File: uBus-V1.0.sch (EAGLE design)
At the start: 13 parts, among them U1 FTS31XS-U, U3 MIC5219 3.3V

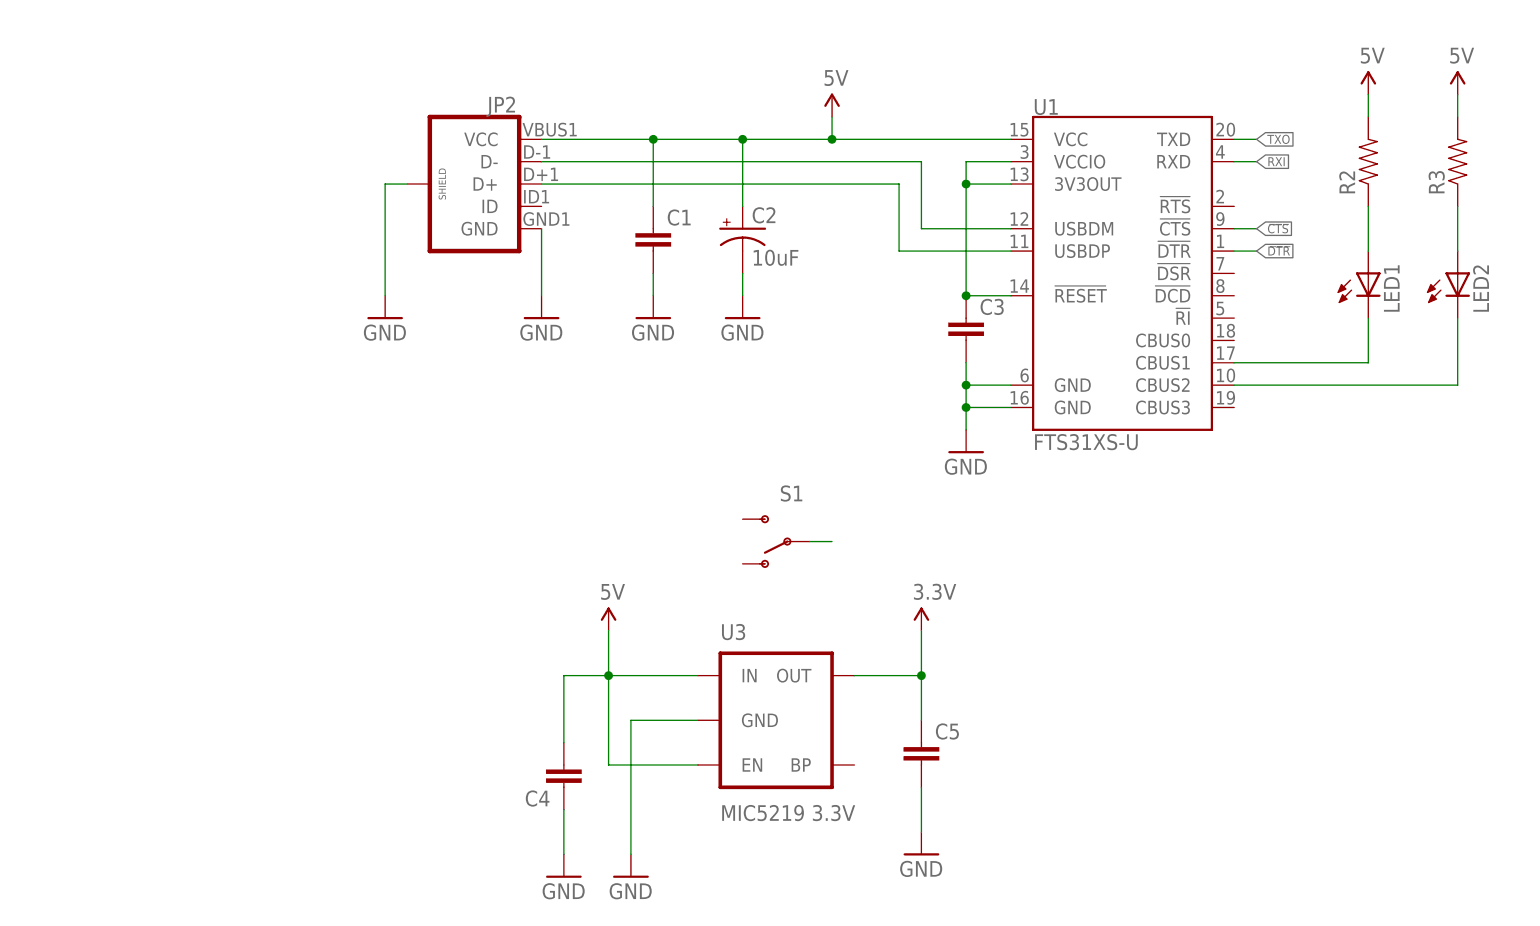
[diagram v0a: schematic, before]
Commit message: Conversor USB-micro a Serial IC. 5V/3.3V compatible
Enrrutado terminado
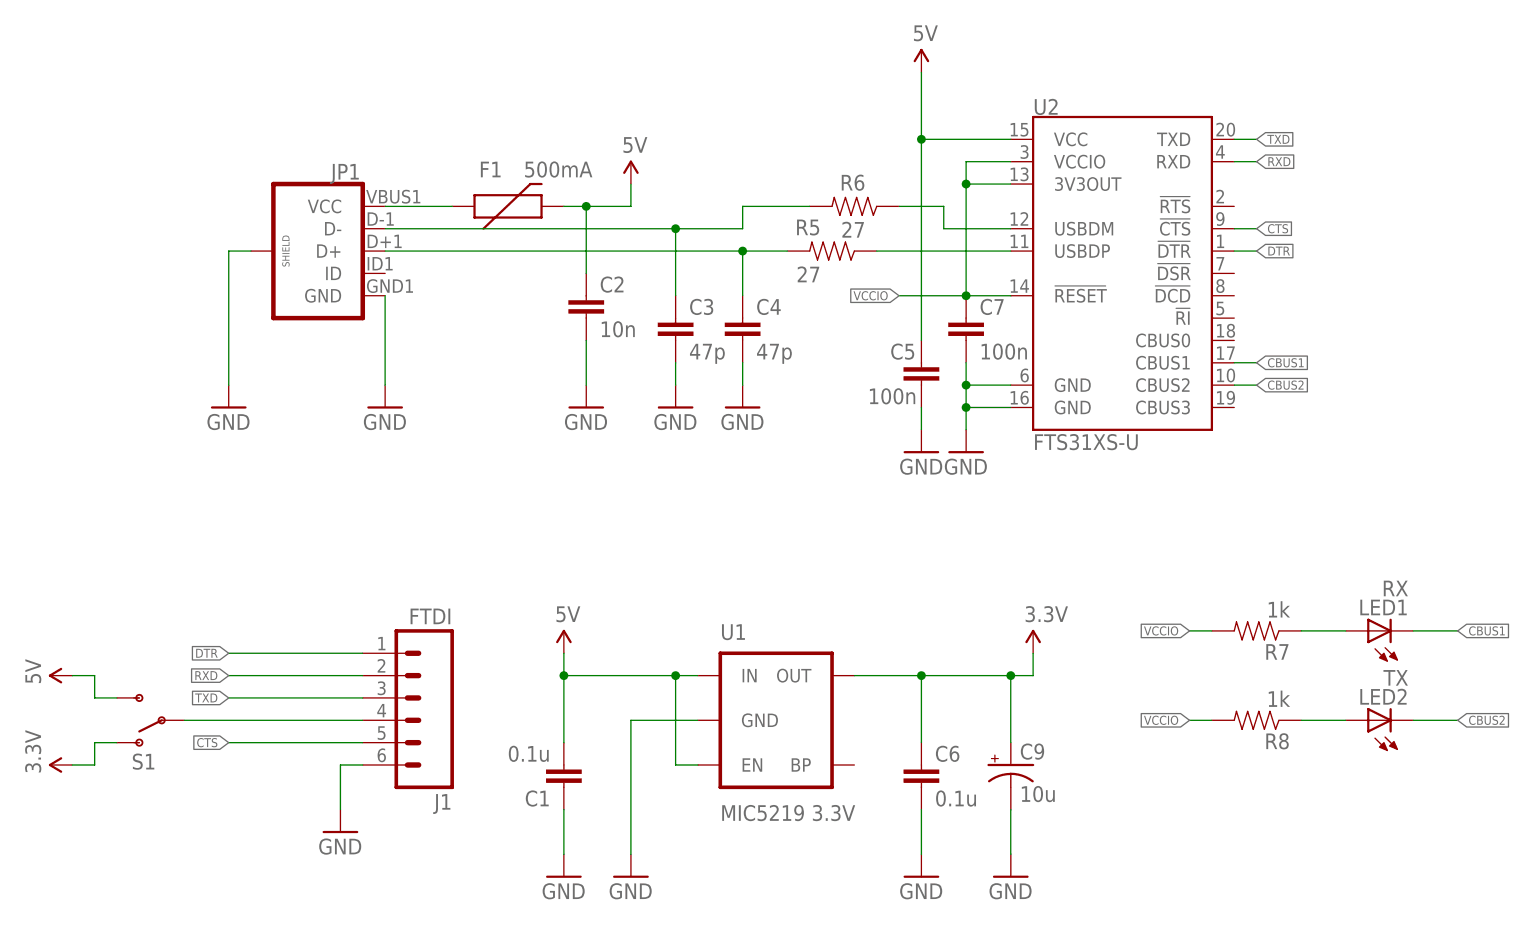
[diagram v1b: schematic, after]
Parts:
- removed JP2: (no value), SparkFun-Connectors:USB_MICROB_PLUGCONN-11752
- removed R2, R3: (no value), SparkFun-Passives:RESISTOR0805-RES
- removed U3: MIC5219 3.3V, SparkFun-PowerIC:V_REG_MIC52193.3V
- added C6: 0.1u, SparkFun-Passives:CAP0603-CAP
- added C7: 100n, SparkFun-Passives:CAP0603-CAP
- added C9: 10u, rcl:CPOL-USSMCP
- added F1: 500mA, SparkFun-PowerIC:PTCSMD
- added J1: FTDI, SparkFun-Connectors:M06LONGPADS
- added JP1: (no value), SparkFun-Connectors:USB_MICROB_PLUGCONN-11752
- added R5, R6: 27, SparkFun-Passives:RESISTOR0603-RES
- added R7, R8: 1k, SparkFun-Passives:RESISTOR0603-RES
- added U2: FTS31XS-U, SparkFun-DigitalIC:FT231XS
- C1: value (none) -> 0.1u; device SparkFun-Passives:CAP0805 -> SparkFun-Passives:CAP0603-CAP
- C2: value 10uF -> 10n; device SparkFun-Capacitors:10UF-16V-10%(TANT) -> SparkFun-Passives:CAP0603-CAP
- C3, C4: value (none) -> 47p; device SparkFun-Passives:CAP0805 -> SparkFun-Passives:CAP0603-CAP
- C5: value (none) -> 100n; device SparkFun-Passives:CAP0805 -> SparkFun-Passives:CAP0603-CAP
- LED1: value (none) -> RX; device led:LEDCHIP-LED0805 -> led:LEDCHIP-LED0603
- LED2: value (none) -> TX; device led:LEDCHIP-LED0805 -> led:LEDCHIP-LED0603
- U1: value FTS31XS-U -> MIC5219 3.3V; device SparkFun-DigitalIC:FT231XS -> SparkFun-PowerIC:V_REG_MIC52193.3V
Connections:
- removed net C̅T̅S̅: U1.!CTS
- removed net D̅T̅R̅: U1.!DTR
- removed net N$2: LED2.C, U1.CBUS2
- removed net N$5: C3.1, U1.!RESET, U1.3V3OUT, U1.VCCIO
- removed net N$6: S1.P
- removed net RXI: U1.RXD
- removed net TXO: U1.TXD
- new net CBUS1: LED1.C, U2.CBUS1
- new net CBUS2: LED2.C, U2.CBUS2
- new net CTS: J1.5, U2.!CTS
- new net DTR: J1.1, U2.!DTR
- new net N$10: C3.1, JP1.D-, R6.2
- new net N$11: F1.1, JP1.VCC
- new net N$7: R6.1, U2.USBDM
- new net RXD: J1.2, U2.RXD
- new net TXD: J1.3, U2.TXD
- new net VCCIO: C7.1, R7.2, R8.2, U2.!RESET, U2.3V3OUT, U2.VCCIO
- net 3.3V: now also C6.1, C9.+, S1.O, U1.OUT; no longer C5.1, U3.OUT
- net 5V: now also C1.2, C2.1, C5.1, F1.2, S1.S, U1.EN, U1.IN, U2.VCC; no longer C1.1, C2.+, C4.2, JP2.VCC, R2.2, R3.2, U1.VCC, U3.EN, U3.IN
- net GND: now also C1.1, C2.2, C4.2, C6.2, C7.2, C9.-, J1.6, JP1.GND, JP1.SHIELD, U1.GND, U2.GND@16, U2.GND@6; no longer C1.2, C2.-, C4.1, JP2.GND, JP2.SHIELD, U1.GND@16, U1.GND@6, U3.GND
- net N$1: now also J1.4, S1.P; no longer LED1.C, U1.CBUS1
- net N$3: now also LED2.A, R8.1; no longer LED1.A, R2.1
- net N$4: now also LED1.A, R7.1; no longer LED2.A, R3.1
- net N$8: now also R5.1, U2.USBDP; no longer JP2.D-, U1.USBDM
- net N$9: now also C4.1, JP1.D+, R5.2; no longer JP2.D+, U1.USBDP
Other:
- moved on the sheet: C1, C3, C4, C5, LED1, LED2, S1
